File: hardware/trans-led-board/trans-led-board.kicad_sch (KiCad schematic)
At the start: 9 parts, among them J1 Conn_01x04

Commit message: Updated notes and metadata
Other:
- note added: "Note: This board is designed for an Aluminum substrate, which requires a single-layer PCB layout. Zero-ohm resistors may be added to the schematic as jumpers where necessary."
- note removed: "Note: Pinout is different from FR4 version, for routing reasons. Make sure to update main board in next revision, as this is likely a cleaner pinout to route regardless."
- title: Printalyzer UV/VIS Densitometer - Transmission LED Al Board -> Printalyzer UV/VIS Densitometer - Transmission LED Board
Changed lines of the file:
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@@
   (paper "USLetter")
   (title_block
-    (title "Printalyzer UV/VIS Densitometer - Transmission LED Al Board")
-    (date "2023-10-08")
-    (rev "A")
+    (title "Printalyzer UV/VIS Densitometer - Transmission LED Board")
+    (date "2023-11-06")
+    (rev "B")
     (company "Dektronics, Inc.")
     (comment 1 "Derek Konigsberg <dkonigsberg@dektronics.com>")
@@
     (effects (font (size 1.27 1.27)) (justify left bottom))
   )
-  (text "Note: Pinout is different from FR4 version, for routing reasons.\nMake sure to update main board in next revision, as this is likely\na cleaner pinout to route regardless."
-    (at 36.83 83.82 0)
+  (text "Note: This board is designed for an Aluminum substrate,\nwhich requires a single-layer PCB layout.\nZero-ohm resistors may be added to the schematic\nas jumpers where necessary."
+    (at 36.83 91.44 0)
     (effects (font (size 1.27 1.27) italic) (justify left bottom))
   )

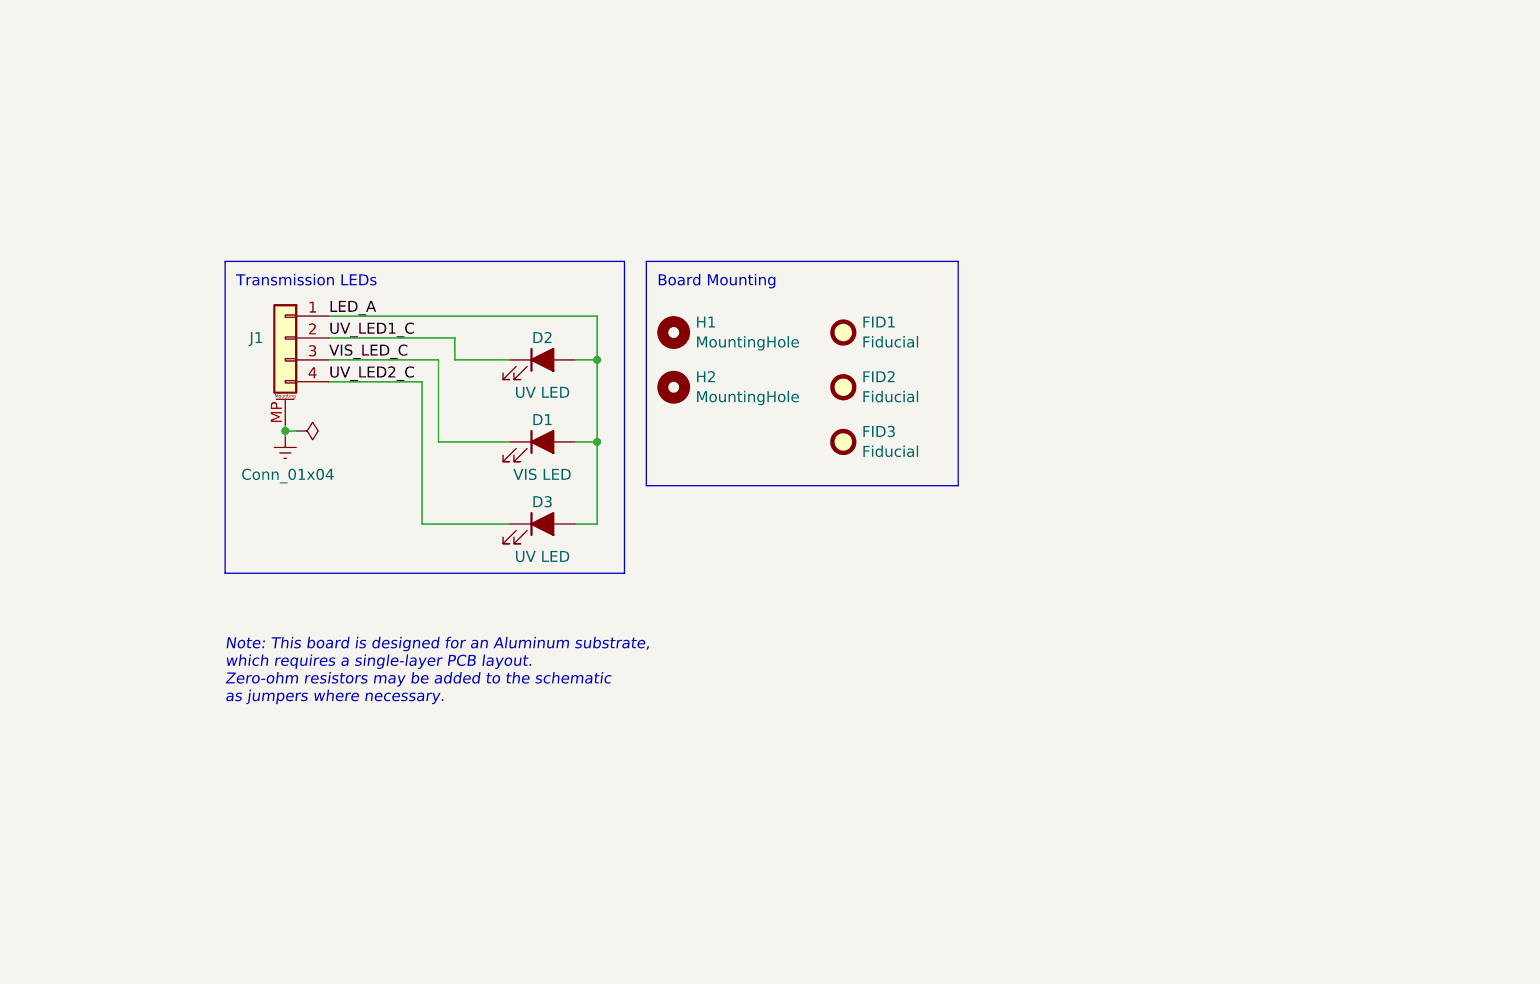
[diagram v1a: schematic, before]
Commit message: Schematic updated to include both LEDs and drivers
There will likely be a lot of back-and-forth updates between the PCB and
schematic during routing.
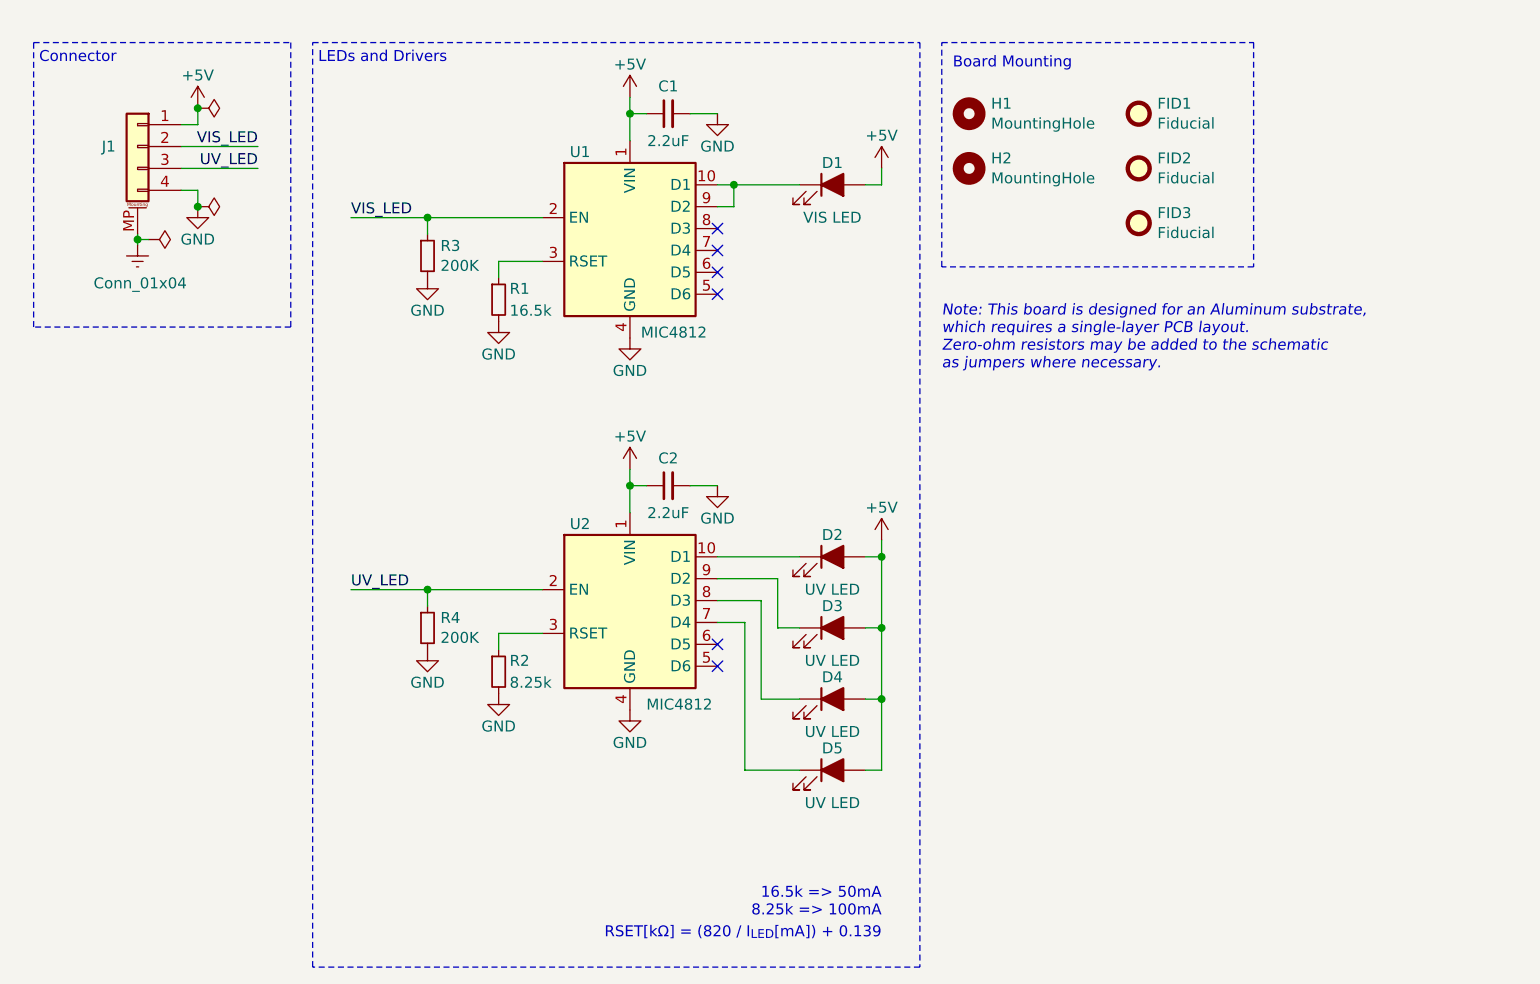
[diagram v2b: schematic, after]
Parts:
- added C1, C2: 2.2uF, Capacitor_SMD:C_0603_1608Metric, symbol Device:C_Small
- added D4, D5: UV LED, lib_fp:LED_WL-SUTW-2835_Narrow, symbol Device:LED_Filled
- added R1: 16.5k, Resistor_SMD:R_0603_1608Metric, symbol Device:R_Small
- added R2: 8.25k, Resistor_SMD:R_0603_1608Metric, symbol Device:R_Small
- added R3, R4: 200K, Resistor_SMD:R_0603_1608Metric, symbol Device:R_Small
- added U1, U2: MIC4812, lib_fp:Micrel_MSOP-10-1EP_3x3mm_P0.5mm_EP1.73x1.7mm, symbol Project:MIC4812
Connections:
- net LED_A renamed +5V
- net +5V: now also C1.1, C2.1, D4.2 (A), D5.2 (A), U1.1 (VIN), U2.1 (VIN)
- net UV_LED1_C: no longer names the net of D2.1 (K)
- net UV_LED1_C: now also U2.10 (D1); no longer J1.2 (Pin_2)
- net UV_LED2_C: no longer names the net of D3.1 (K)
- net UV_LED2_C: now also U2.9 (D2); no longer J1.4 (Pin_4)
- net VIS_LED_C: no longer names the net of D1.1 (K)
- net VIS_LED_C: now also U1.10 (D1), U1.9 (D2); no longer J1.3 (Pin_3)
- new net: D4.1 (K), U2.8 (D3)
- new net: R1.1, U1.3 (RSET)
- new net: R2.1, U2.3 (RSET)
- new net: D5.1 (K), U2.7 (D4)
- new net GND: C1.2, C2.2, J1.4 (Pin_4), R1.2, R2.2, R3.2, R4.2, U1.11 (EP), U1.4 (GND), U2.11 (EP), U2.4 (GND)
- new net UV_LED: J1.3 (Pin_3), R4.1, U2.2 (EN)
- new net VIS_LED: J1.2 (Pin_2), R3.1, U1.2 (EN)
- no-connect marks 0 -> 6
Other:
- note added: "16.5k => 50mA 8.25k => 100mA"
- note added: "Connector"
- note added: "LEDs and Drivers"
- note added: "RSET[kΩ] = (820 / I_{LED}[mA]) + 0.139"
- note removed: "Transmission LEDs"
- moved on the sheet: D1, D2, D3, FID1, FID2, FID3, H1, H2, J1

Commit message: Updated transmission LED board now fully routed
Still a lot of cleanup and organization work necessary
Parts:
- added R5, R6: 0R, Resistor_SMD:R_0603_1608Metric, symbol Device:R_Small
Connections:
- net +5V: now also J1.4 (Pin_4); no longer J1.1 (Pin_1)
- net GND: now also J1.1 (Pin_1); no longer J1.4 (Pin_4)
- net UV_LED: now also J1.2 (Pin_2), R6.1; no longer J1.3 (Pin_3), U2.2 (EN)
- net VIS_LED: now also J1.3 (Pin_3), R5.1; no longer J1.2 (Pin_2), U1.2 (EN)
- net at D4.1 (K): now also U2.9 (D2); no longer U2.8 (D3)
- net at U2.10 (D1): now also D5.1 (K); no longer D2.1 (K)
- net at U2.7 (D4): now also D2.1 (K); no longer D5.1 (K)
- net at D3.1 (K): now also U2.8 (D3); no longer U2.9 (D2)
- new net: R5.2, U1.2 (EN)
- new net: R6.2, U2.2 (EN)
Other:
- note added: "--> Clean up pin assignment symbols"
- moved on the sheet: D2, D3, D4, D5

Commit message: Transmission LED board rounding cleaned up
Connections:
- net D1_C: now reaches D1.1 (K), U1.10 (D1), U1.9 (D2)
- net D4_C: now reaches D4.1 (K), U2.9 (D2)
- net D5_C: now reaches D5.1 (K), U2.10 (D1)
- net D2_C: now reaches D2.1 (K), U2.7 (D4)
- net D3_C: now reaches D3.1 (K), U2.8 (D3)
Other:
- note removed: "--> Clean up pin assignment symbols"
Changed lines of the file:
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@@
   (junction (at 113.03 82.55) (diameter 0) (color 0 0 0 0)
   )
+  (junction (at 38.735 19.685) (diameter 0) (color 0 0 0 0)
+  )
   (junction (at 113.03 74.295) (diameter 0) (color 0 0 0 0)
   )
-  (junction (at 33.655 33.655) (diameter 0) (color 0 0 0 0)
+  (junction (at 38.735 34.925) (diameter 0) (color 0 0 0 0)
   )
   (junction (at 95.885 31.115) (diameter 0) (color 0 0 0 0)
   )
   (junction (at 60.325 34.925) (diameter 0) (color 0 0 0 0)
-  )
-  (junction (at 33.655 22.225) (diameter 0) (color 0 0 0 0)
   )
   (junction (at 83.82 22.86) (diameter 0) (color 0 0 0 0)
@@
     (stroke (width 0) (type default))
   )
+  (wire (pts (xy 33.655 34.925) (xy 38.735 34.925))
+    (stroke (width 0) (type default))
+  )
   (wire (pts (xy 83.82 22.86) (xy 83.82 26.035))
     (stroke (width 0) (type default))
@@
     (stroke (width 0) (type default))
   )
-  (wire (pts (xy 33.655 31.75) (xy 33.655 33.655))
+  (wire (pts (xy 33.655 31.75) (xy 33.655 34.925))
     (stroke (width 0) (type default))
   )
@@
     (stroke (width 0) (type default))
   )
+  (wire (pts (xy 33.655 19.685) (xy 38.735 19.685))
+    (stroke (width 0) (type default))
+  )
   (wire (pts (xy 97.155 81.915) (xy 93.98 81.915))
     (stroke (width 0) (type default))
@@
     (stroke (width 0) (type default))
   )
-  (wire (pts (xy 33.655 22.225) (xy 33.655 24.13))
+  (wire (pts (xy 33.655 19.685) (xy 33.655 24.13))
     (stroke (width 0) (type default))
   )
@@
     (fill (type none))
   )
-  (rectangle (start 46.99 14.605) (end 117.475 121.92)
+  (rectangle (start 46.99 14.605) (end 117.475 114.935)
     (stroke (width 0) (type dash))
     (fill (type none))
   )
-  (text "Connector" (at 15.24 17.145 0)
+  (text "Connector" (at 15.875 17.78 0)
     (effects (font (size 1.27 1.27)) (justify left bottom))
   )
-  (text "LEDs and Drivers" (at 47.625 17.145 0)
+  (text "LEDs and Drivers" (at 48.26 17.78 0)
     (effects (font (size 1.27 1.27)) (justify left bottom))
   )
-  (text "RSET[kΩ] = (820 / I_{LED}[mA]) + 0.139" (at 113.03 118.745 0)
+  (text "RSET[kΩ] = (820 / I_{LED}[mA]) + 0.139" (at 113.03 113.03 0)
     (effects (font (size 1.27 1.27)) (justify right bottom))
   )
@@
     (effects (font (size 1.27 1.27) italic) (justify left bottom))
   )
-  (text "16.5k => 50mA\n8.25k => 100mA" (at 113.03 116.205 0)
+  (text "16.5k => 50mA\n8.25k => 100mA" (at 113.03 110.49 0)
     (effects (font (size 1.27 1.27)) (justify right bottom))
   )
-  (text "--> Clean up pin assignment symbols" (at 12.7 13.97 0)
+  (label "D4_C" (at 93.98 76.835 0) (fields_autoplaced)
     (effects (font (size 1.27 1.27)) (justify left bottom))
   )
@@
     (effects (font (size 1.27 1.27)) (justify left bottom))
   )
+  (label "D5_C" (at 93.98 74.295 0) (fields_autoplaced)
+    (effects (font (size 1.27 1.27)) (justify left bottom))
+  )
+  (label "D1_C" (at 97.79 31.115 0) (fields_autoplaced)
+    (effects (font (size 1.27 1.27)) (justify left bottom))
+  )
   (label "UV_LED" (at 51.435 78.105 0) (fields_autoplaced)
     (effects (font (size 1.27 1.27)) (justify left bottom))
   )
+  (label "D3_C" (at 93.98 79.375 0) (fields_autoplaced)
+    (effects (font (size 1.27 1.27)) (justify left bottom))
+  )
   (label "UV_LED" (at 40.64 26.67 180) (fields_autoplaced)
     (effects (font (size 1.27 1.27)) (justify right bottom))
+  )
+  (label "D2_C" (at 93.98 81.915 0) (fields_autoplaced)
+    (effects (font (size 1.27 1.27)) (justify left bottom))
   )
   (symbol (lib_id "Device:LED_Filled") (at 107.315 31.115 0) (unit 1)
@@
     )
   )
-  (symbol (lib_id "power:GND") (at 33.655 22.225 180) (unit 1)
-    (in_bom yes) (on_board yes) (dnp no)
-    (property "Reference" "#PWR015" (at 33.655 15.875 0)
-      (effects (font (size 1.27 1.27)) hide)
-    )
-    (property "Value" "GND" (at 33.655 18.415 0)
-      (effects (font (size 1.27 1.27)))
-    )
-    (property "Footprint" "" (at 33.655 22.225 0)
-      (effects (font (size 1.27 1.27)) hide)
-    )
-    (property "Datasheet" "" (at 33.655 22.225 0)
+  (symbol (lib_id "power:GND") (at 38.735 19.685 0) (unit 1)
+    (in_bom yes) (on_board yes) (dnp no)
+    (property "Reference" "#PWR015" (at 38.735 26.035 0)
+      (effects (font (size 1.27 1.27)) hide)
+    )
+    (property "Value" "GND" (at 38.735 23.495 0)
+      (effects (font (size 1.27 1.27)))
+    )
+    (property "Footprint" "" (at 38.735 19.685 0)
+      (effects (font (size 1.27 1.27)) hide)
+    )
+    (property "Datasheet" "" (at 38.735 19.685 0)
       (effects (font (size 1.27 1.27)) hide)
     )
@@
     )
   )
-  (symbol (lib_id "power:+5V") (at 33.655 33.655 180) (unit 1)
-    (in_bom yes) (on_board yes) (dnp no)
-    (property "Reference" "#PWR014" (at 33.655 29.845 0)
-      (effects (font (size 1.27 1.27)) hide)
-    )
-    (property "Value" "+5V" (at 33.655 37.465 0)
-      (effects (font (size 1.27 1.27)))
-    )
-    (property "Footprint" "" (at 33.655 33.655 0)
-      (effects (font (size 1.27 1.27)) hide)
-    )
-    (property "Datasheet" "" (at 33.655 33.655 0)
+  (symbol (lib_id "power:+5V") (at 38.735 34.925 0) (unit 1)
+    (in_bom yes) (on_board yes) (dnp no)
+    (property "Reference" "#PWR014" (at 38.735 38.735 0)
+      (effects (font (size 1.27 1.27)) hide)
+    )
+    (property "Value" "+5V" (at 38.735 31.115 0)
+      (effects (font (size 1.27 1.27)))
+    )
+    (property "Footprint" "" (at 38.735 34.925 0)
+      (effects (font (size 1.27 1.27)) hide)
+    )
+    (property "Datasheet" "" (at 38.735 34.925 0)
       (effects (font (size 1.27 1.27)) hide)
     )
@@
     )
   )
-  (symbol (lib_id "power:PWR_FLAG") (at 33.655 33.655 270) (unit 1)
+  (symbol (lib_id "power:PWR_FLAG") (at 38.735 34.925 180) (unit 1)
     (in_bom yes) (on_board yes) (dnp no) (fields_autoplaced)
-    (property "Reference" "#FLG02" (at 35.56 33.655 0)
-      (effects (font (size 1.27 1.27)) hide)
-    )
-    (property "Value" "PWR_FLAG" (at 36.83 33.655 90)
+    (property "Reference" "#FLG02" (at 38.735 36.83 0)
+      (effects (font (size 1.27 1.27)) hide)
+    )
+    (property "Value" "PWR_FLAG" (at 38.735 38.1 90)
       (effects (font (size 1.27 1.27)) (justify left) hide)
     )
-    (property "Footprint" "" (at 33.655 33.655 0)
-      (effects (font (size 1.27 1.27)) hide)
-    )
-    (property "Datasheet" "~" (at 33.655 33.655 0)
-      (effects (font (size 1.27 1.27)) hide)
-    )
-    (property "Description" "" (at 33.655 33.655 0)
-      (effects (font (size 1.27 1.27)) hide)
-    )
-    (property "Manufacturer" "" (at 33.655 33.655 0)
-      (effects (font (size 1.27 1.27)) hide)
-    )
-    (property "Manufacturer PN" "" (at 33.655 33.655 0)
-      (effects (font (size 1.27 1.27)) hide)
-    )
-    (property "Supplier" "" (at 33.655 33.655 0)
-      (effects (font (size 1.27 1.27)) hide)
-    )
-    (property "Supplier PN" "" (at 33.655 33.655 0)
+    (property "Footprint" "" (at 38.735 34.925 0)
+      (effects (font (size 1.27 1.27)) hide)
+    )
+    (property "Datasheet" "~" (at 38.735 34.925 0)
+      (effects (font (size 1.27 1.27)) hide)
+    )
+    (property "Description" "" (at 38.735 34.925 0)
+      (effects (font (size 1.27 1.27)) hide)
+    )
+    (property "Manufacturer" "" (at 38.735 34.925 0)
+      (effects (font (size 1.27 1.27)) hide)
+    )
+    (property "Manufacturer PN" "" (at 38.735 34.925 0)
+      (effects (font (size 1.27 1.27)) hide)
+    )
+    (property "Supplier" "" (at 38.735 34.925 0)
+      (effects (font (size 1.27 1.27)) hide)
+    )
+    (property "Supplier PN" "" (at 38.735 34.925 0)
       (effects (font (size 1.27 1.27)) hide)
     )
@@
     )
   )
-  (symbol (lib_id "power:PWR_FLAG") (at 33.655 22.225 270) (unit 1)
+  (symbol (lib_id "power:PWR_FLAG") (at 38.735 19.685 0) (unit 1)
     (in_bom yes) (on_board yes) (dnp no) (fields_autoplaced)
-    (property "Reference" "#FLG03" (at 35.56 22.225 0)
-      (effects (font (size 1.27 1.27)) hide)
-    )
-    (property "Value" "PWR_FLAG" (at 36.83 22.225 90)
+    (property "Reference" "#FLG03" (at 38.735 17.78 0)
+      (effects (font (size 1.27 1.27)) hide)
+    )
+    (property "Value" "PWR_FLAG" (at 38.735 16.51 90)
       (effects (font (size 1.27 1.27)) (justify left) hide)
     )
-    (property "Footprint" "" (at 33.655 22.225 0)
-      (effects (font (size 1.27 1.27)) hide)
-    )
-    (property "Datasheet" "~" (at 33.655 22.225 0)
-      (effects (font (size 1.27 1.27)) hide)
-    )
-    (property "Description" "" (at 33.655 22.225 0)
-      (effects (font (size 1.27 1.27)) hide)
-    )
-    (property "Manufacturer" "" (at 33.655 22.225 0)
-      (effects (font (size 1.27 1.27)) hide)
-    )
-    (property "Manufacturer PN" "" (at 33.655 22.225 0)
-      (effects (font (size 1.27 1.27)) hide)
-    )
-    (property "Supplier" "" (at 33.655 22.225 0)
-      (effects (font (size 1.27 1.27)) hide)
-    )
-    (property "Supplier PN" "" (at 33.655 22.225 0)
-      (effects (font (size 1.27 1.27)) hide)
-    )
+    (property "Footprint" "" (at 38.735 19.685 0)
+      (effects (font (size 1.27 1.27)) hide)
+    )
+    (property "Datasheet" "~" (at 38.735 19.685 0)
+      (effects (font (size 1.27 1.27)) hide)
+    )
+    (property "Description" "" (at 38.735 19.685 0)
+      (effects (font (size 1.27 1.27)) hide)
+    )
+    (property "Manufacturer" "" (at 38.735 19.685 0)
+      (effects (font (size 1.27 1.27)) hide)
+    )
+    (property "Manufacturer PN" "" (at 38.735 19.685 0)
+      (effects (font (size 1.27 1.27)) hide)
+    )
+    (property "Supplier" "" (at 38.735 19.685 0)
+      (effects (font (size 1.27 1.27)) hide)
+    )
+    (property "Supplier PN" "" (at 38.735 19.685 0)
+      (effects (font (size 1.27 1.27)) hide)
+    )
